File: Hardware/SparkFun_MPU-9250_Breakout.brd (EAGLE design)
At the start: 17 x 17.8 mm, 18 parts, among them U1 MPU-9250

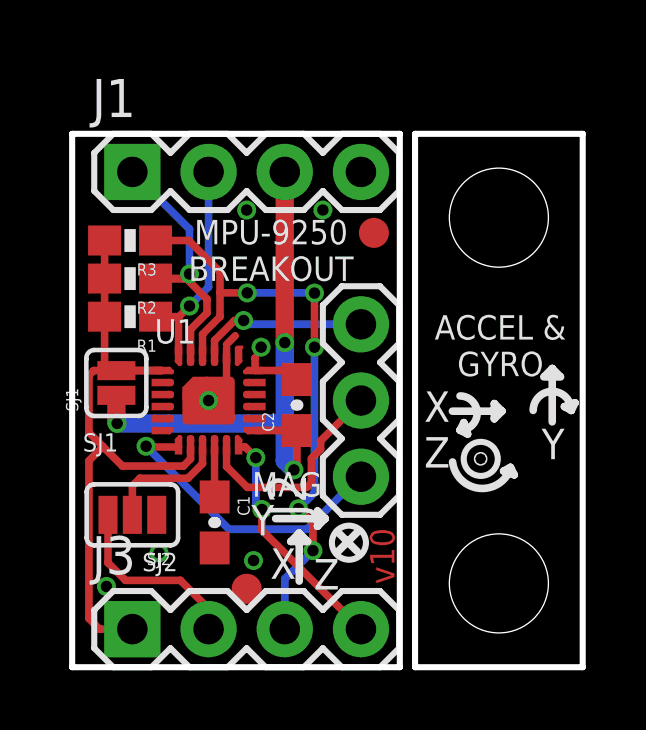
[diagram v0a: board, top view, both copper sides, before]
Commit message: Removed exposed pad copper from PCB
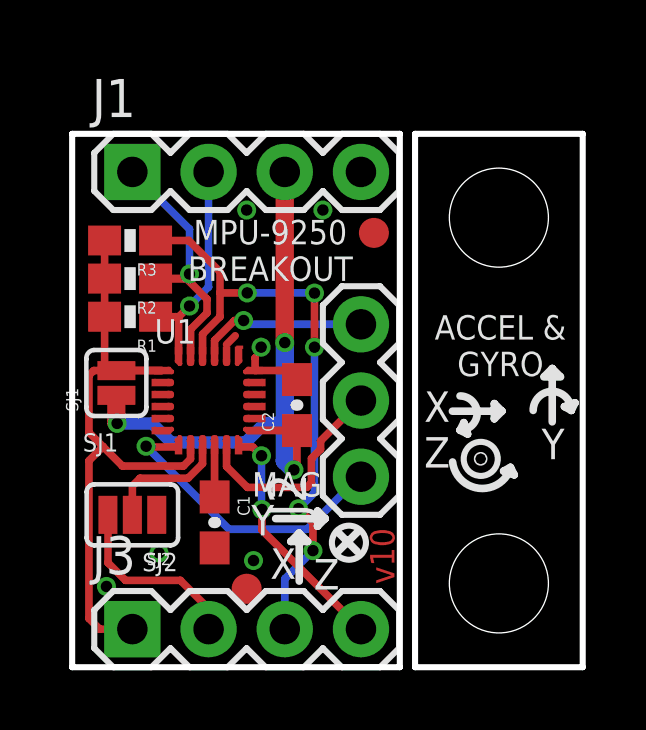
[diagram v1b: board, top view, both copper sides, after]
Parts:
- U1: device Testing:QFN24_PAD -> Testing:QFN24
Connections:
- net GND: no longer U1.CENTER
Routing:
- net GND: track 5.03 -> 2.85 mm, vias 7 -> 6
- net VDD: track 19.4 -> 19.9 mm
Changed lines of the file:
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@@
 <setting verticaltext="up"/>
 </settings>
-<grid distance="0.001" unitdist="inch" unit="inch" style="lines" multiple="1" display="yes" altdistance="0.025" altunitdist="inch" altunit="inch"/>
+<grid distance="0.0025" unitdist="inch" unit="inch" style="lines" multiple="1" display="yes" altdistance="0.025" altunitdist="inch" altunit="inch"/>
 <layers>
 <layer number="1" name="Top" color="4" fill="1" visible="yes" active="yes"/>
@@
 <wire x1="8.8646" y1="3.8608" x2="9.4996" y2="4.4958" width="0.254" layer="21"/>
 <text x="2.54" y="12.4714" size="0.8128" layer="22" font="vector" ratio="15" rot="SMR0" align="center-left">A&amp;G</text>
-<text x="6.6294" y="13.8938" size="0.8128" layer="21" font="vector" ratio="15" align="center">MPU-9250
+<text x="6.604" y="13.8938" size="0.8128" layer="21" font="vector" ratio="15" align="center">MPU-9250
 BREAKOUT</text>
 <rectangle x1="6.32" y1="8.165" x2="6.45" y2="8.415" layer="1"/>
@@
 <elements>
 <element name="FRAME1" library="SparkFun-Aesthetics" package="CREATIVE_COMMONS" value="FRAME-LETTER" x="-21.8694" y="-13.4112"/>
-<element name="U1" library="Testing" package="QFN24_PAD" value="MPU-9250" x="4.5466" y="8.89">
+<element name="U1" library="Testing" package="QFN24" value="MPU-9250" x="4.5466" y="8.89">
 <attribute name="PROD_ID" value="IC-13192" x="4.5466" y="8.89" size="1.778" layer="27" display="off"/>
 </element>
@@
 <contactref element="U1" pad="20"/>
 <contactref element="U1" pad="18"/>
-<contactref element="U1" pad="CENTER"/>
-<wire x1="5.1466" y1="10.44" x2="5.1466" y2="9.49" width="0.254" layer="1"/>
-<wire x1="5.1466" y1="9.49" x2="4.5466" y2="8.89" width="0.254" layer="1"/>
 <contactref element="C1" pad="2"/>
 <contactref element="C2" pad="2"/>
@@
 <wire x1="6.0966" y1="9.89" x2="6.0966" y2="10.3118" width="0.254" layer="1"/>
 <wire x1="6.0966" y1="10.3118" x2="6.096" y2="10.3124" width="0.254" layer="1"/>
-<via x="4.5466" y="8.89" extent="1-16" drill="0.381"/>
 <polygon width="0.2032" layer="16" isolate="0.3048">
 <vertex x="0" y="0"/>
@@
 <via x="6.2992" y="10.668" extent="1-16" drill="0.381"/>
 <via x="1.143" y="2.6924" extent="1-16" drill="0.381"/>
-<wire x1="4.1656" y1="8.89" x2="4.5466" y2="8.89" width="0.254" layer="1"/>
 <wire x1="6.0966" y1="9.89" x2="7.493" y2="9.89" width="0.254" layer="1"/>
 <wire x1="7.493" y1="9.89" x2="7.493" y2="9.5876" width="0.254" layer="1"/>
@@
 <wire x1="7.0866" y1="16.51" x2="7.0866" y2="10.8204" width="0.6096" layer="1"/>
 <via x="7.0866" y="10.8204" extent="1-16" drill="0.381"/>
-<wire x1="7.0866" y1="10.8204" x2="7.0866" y2="8.1788" width="0.6096" layer="16"/>
-<wire x1="7.0866" y1="8.1788" x2="7.0866" y2="6.8834" width="0.6096" layer="16"/>
+<wire x1="7.0866" y1="10.8204" x2="7.0866" y2="8.144353125" width="0.6096" layer="16"/>
+<wire x1="7.0866" y1="8.144353125" x2="7.0866" y2="6.8834" width="0.6096" layer="16"/>
 <wire x1="7.0866" y1="6.8834" x2="7.3914" y2="6.5786" width="0.6096" layer="16"/>
 <wire x1="1.4732" y1="9.0623" x2="1.4732" y2="8.1534" width="0.6096" layer="1"/>
 <wire x1="1.4732" y1="8.1534" x2="1.4986" y2="8.128" width="0.6096" layer="1"/>
 <via x="1.4986" y="8.128" extent="1-16" drill="0.381"/>
-<wire x1="1.4986" y1="8.128" x2="7.0358" y2="8.128" width="0.6096" layer="16"/>
-<wire x1="7.0358" y1="8.128" x2="7.0866" y2="8.1788" width="0.6096" layer="16"/>
+<wire x1="1.4986" y1="8.128" x2="2.667" y2="8.128" width="0.4064" layer="16"/>
+<wire x1="3.302" y1="7.493" x2="5.7785" y2="7.493" width="0.4064" layer="16"/>
+<wire x1="2.667" y1="8.128" x2="3.302" y2="7.493" width="0.4064" layer="16"/>
+<wire x1="5.7785" y1="7.493" x2="6.429853125" y2="8.144353125" width="0.4064" layer="16"/>
+<wire x1="7.0866" y1="8.144353125" x2="6.429853125" y2="8.144353125" width="0.4064" layer="16"/>
 </signal>
 <signal name="VDDIO">
@@
 <contactref element="U1" pad="12"/>
 <contactref element="J3" pad="4"/>
-<wire x1="5.5466" y1="7.34" x2="5.7664" y2="7.34" width="0.254" layer="1"/>
-<wire x1="5.7664" y1="7.34" x2="6.1214" y2="6.985" width="0.254" layer="1"/>
-<via x="6.1214" y="6.985" extent="1-16" drill="0.381"/>
-<wire x1="6.1214" y1="6.985" x2="6.1214" y2="5.461" width="0.254" layer="16"/>
-<wire x1="6.1214" y1="5.461" x2="6.3246" y2="5.2578" width="0.254" layer="16"/>
+<wire x1="5.5466" y1="7.34" x2="6.0204" y2="7.34" width="0.254" layer="1"/>
+<wire x1="6.0204" y1="7.34" x2="6.3119" y2="7.0485" width="0.254" layer="1"/>
+<via x="6.3119" y="7.0485" extent="1-16" drill="0.381"/>
+<wire x1="6.3119" y1="7.0485" x2="6.3119" y2="5.2705" width="0.254" layer="16"/>
 <via x="6.3246" y="5.2578" extent="1-16" drill="0.381"/>
 <wire x1="6.3246" y1="5.2578" x2="6.3246" y2="4.572" width="0.254" layer="1"/>
 <wire x1="6.3246" y1="4.572" x2="9.6266" y2="1.27" width="0.254" layer="1"/>
+<wire x1="6.3119" y1="5.2705" x2="6.3246" y2="5.2578" width="0.254" layer="16"/>
 </signal>
 <signal name="FSYNC">
